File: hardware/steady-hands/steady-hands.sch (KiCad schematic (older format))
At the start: 16 parts, among them J1 SWD, J2 UART, J3 I2C, SW1 SW_Push, SW2 SW_SPDT, U1 STM32F411CEUx

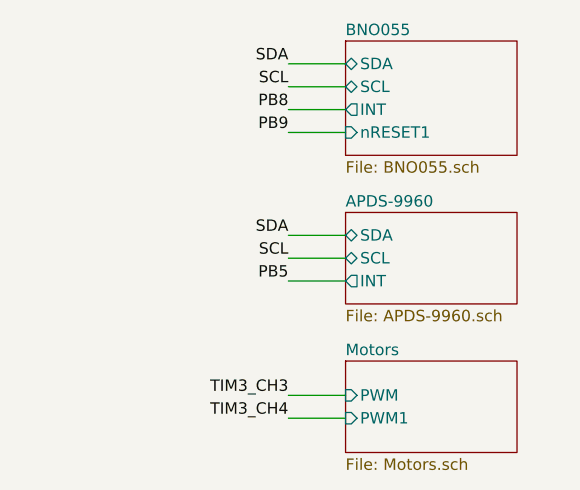
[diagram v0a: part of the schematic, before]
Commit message: Adds footprints
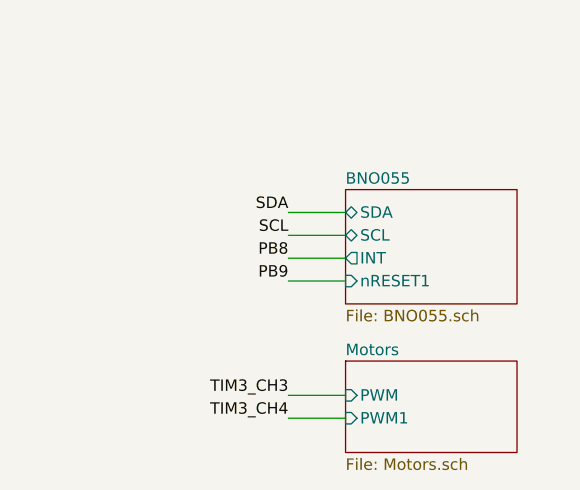
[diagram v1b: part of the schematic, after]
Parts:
- C1, C2, C3, C4, C5, C6, C7, C8, C9: footprint (none) -> Capacitor_SMD:C_0402_1005Metric
- J1: footprint (none) -> Connector_PinHeader_2.54mm:PinHeader_1x04_P2.54mm_Vertical
- J2: footprint (none) -> Connector_PinHeader_2.54mm:PinHeader_1x05_P2.54mm_Vertical
- J3: footprint (none) -> Connector_PinHeader_2.54mm:PinHeader_1x06_P2.54mm_Vertical
- R1: footprint (none) -> Resistor_SMD:R_0402_1005Metric
- SW1: footprint (none) -> Button_Switch_SMD:SW_SPST_B3SL-1002P
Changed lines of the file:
@@
 $Descr A4 11693 8268
 encoding utf-8
-Sheet 1 7
+Sheet 1 6
 Title ""
 Date ""
@@
 TIM3_CH3
 Wire Wire Line
-	9000 1550 8750 1550
-Wire Wire Line
-	9000 1650 8750 1650
-Wire Wire Line
-	9000 1750 8750 1750
-Text Label 8750 1550 2    50   ~ 0
+	9000 2200 8750 2200
+Wire Wire Line
+	9000 2300 8750 2300
+Wire Wire Line
+	9000 2400 8750 2400
+Text Label 8750 2200 2    50   ~ 0
 SDA
-Text Label 8750 1650 2    50   ~ 0
+Text Label 8750 2300 2    50   ~ 0
 SCL
-Text Label 8750 1750 2    50   ~ 0
+Text Label 8750 2400 2    50   ~ 0
 PB8
-$Sheet
-S 9000 2200 750  400
-U 5EF838FE
-F0 "APDS-9960" 50
-F1 "APDS-9960.sch" 50
-F2 "SDA" B L 9000 2300 50
-F3 "SCL" B L 9000 2400 50
-F4 "INT" O L 9000 2500 50
-$EndSheet
-Wire Wire Line
-	9000 2300 8750 2300
-Wire Wire Line
-	9000 2400 8750 2400
-Wire Wire Line
-	9000 2500 8750 2500
-Text Label 8750 2300 2    50   ~ 0
-SDA
-Text Label 8750 2400 2    50   ~ 0
-SCL
-Text Label 8750 2500 2    50   ~ 0
-PB5
 $Comp
 L MCU_ST_STM32F4:STM32F411CEUx U1
@@
 PB4
 Wire Wire Line
-	9000 1850 8750 1850
-Text Label 8750 1850 2    50   ~ 0
+	9000 2500 8750 2500
+Text Label 8750 2500 2    50   ~ 0
 PB9
 Wire Wire Line
@@
 F 0 "C1" H 2015 3746 50  0000 L CNN
 F 1 "0.1u" H 2015 3655 50  0000 L CNN
-F 2 "" H 1938 3550 50  0001 C CNN
+F 2 "Capacitor_SMD:C_0402_1005Metric" H 1938 3550 50  0001 C CNN
 F 3 "~" H 1900 3700 50  0001 C CNN
 	1    1900 3700
@@
 F 0 "SW1" V 1446 3652 50  0000 R CNN
 F 1 "SW_Push" V 1355 3652 50  0000 R CNN
-F 2 "" H 1400 3900 50  0001 C CNN
+F 2 "Button_Switch_SMD:SW_SPST_B3SL-1002P" H 1400 3900 50  0001 C CNN
 F 3 "~" H 1400 3900 50  0001 C CNN
 	1    1400 3700
@@
 F 0 "C3" H 2565 4096 50  0000 L CNN
 F 1 "4.7u" H 2565 4005 50  0000 L CNN
-F 2 "" H 2488 3900 50  0001 C CNN
+F 2 "Capacitor_SMD:C_0402_1005Metric" H 2488 3900 50  0001 C CNN
 F 3 "~" H 2450 4050 50  0001 C CNN
 	1    2450 4050
@@
 F 0 "C2" H 2265 1996 50  0000 L CNN
 F 1 "100n" H 2265 1905 50  0000 L CNN
-F 2 "" H 2188 1800 50  0001 C CNN
+F 2 "Capacitor_SMD:C_0402_1005Metric" H 2188 1800 50  0001 C CNN
 F 3 "~" H 2150 1950 50  0001 C CNN
 	1    2150 1950
@@
 F 0 "C4" H 2715 1996 50  0000 L CNN
 F 1 "100n" H 2715 1905 50  0000 L CNN
-F 2 "" H 2638 1800 50  0001 C CNN
+F 2 "Capacitor_SMD:C_0402_1005Metric" H 2638 1800 50  0001 C CNN
 F 3 "~" H 2600 1950 50  0001 C CNN
 	1    2600 1950
@@
 F 0 "C5" H 3165 1996 50  0000 L CNN
 F 1 "100n" H 3165 1905 50  0000 L CNN
-F 2 "" H 3088 1800 50  0001 C CNN
+F 2 "Capacitor_SMD:C_0402_1005Metric" H 3088 1800 50  0001 C CNN
 F 3 "~" H 3050 1950 50  0001 C CNN
 	1    3050 1950
@@
 F 0 "C6" H 3615 1996 50  0000 L CNN
 F 1 "100n" H 3615 1905 50  0000 L CNN
-F 2 "" H 3538 1800 50  0001 C CNN
+F 2 "Capacitor_SMD:C_0402_1005Metric" H 3538 1800 50  0001 C CNN
 F 3 "~" H 3500 1950 50  0001 C CNN
 	1    3500 1950
@@
 F 0 "C7" H 4065 1996 50  0000 L CNN
 F 1 "4.7u" H 4065 1905 50  0000 L CNN
-F 2 "" H 3988 1800 50  0001 C CNN
+F 2 "Capacitor_SMD:C_0402_1005Metric" H 3988 1800 50  0001 C CNN
 F 3 "~" H 3950 1950 50  0001 C CNN
 	1    3950 1950
@@
 F 0 "C8" H 4715 1996 50  0000 L CNN
 F 1 "100n" H 4715 1905 50  0000 L CNN
-F 2 "" H 4638 1800 50  0001 C CNN
+F 2 "Capacitor_SMD:C_0402_1005Metric" H 4638 1800 50  0001 C CNN
 F 3 "~" H 4600 1950 50  0001 C CNN
 	1    4600 1950
@@
 F 0 "C9" H 5165 1996 50  0000 L CNN
 F 1 "1u" H 5165 1905 50  0000 L CNN
-F 2 "" H 5088 1800 50  0001 C CNN
+F 2 "Capacitor_SMD:C_0402_1005Metric" H 5088 1800 50  0001 C CNN
 F 3 "~" H 5050 1950 50  0001 C CNN
 	1    5050 1950
@@
 F 0 "R1" H 2720 5646 50  0000 L CNN
 F 1 "10k" H 2720 5555 50  0000 L CNN
-F 2 "" V 2580 5600 50  0001 C CNN
+F 2 "Resistor_SMD:R_0402_1005Metric" V 2580 5600 50  0001 C CNN
 F 3 "~" H 2650 5600 50  0001 C CNN
 	1    2650 5600
@@
 F 0 "J1" H 7030 2942 50  0000 L CNN
 F 1 "SWD" H 7030 2851 50  0000 L CNN
-F 2 "" H 6950 2950 50  0001 C CNN
+F 2 "Connector_PinHeader_2.54mm:PinHeader_1x04_P2.54mm_Vertical" H 6950 2950 50  0001 C CNN
 F 3 "~" H 6950 2950 50  0001 C CNN
 	1    6950 2950
@@
 F 0 "J2" H 7030 4092 50  0000 L CNN
 F 1 "UART" H 7030 4001 50  0000 L CNN
-F 2 "" H 6950 4050 50  0001 C CNN
+F 2 "Connector_PinHeader_2.54mm:PinHeader_1x05_P2.54mm_Vertical" H 6950 4050 50  0001 C CNN
 F 3 "~" H 6950 4050 50  0001 C CNN
 	1    6950 4050
@@
 F 0 "J3" H 7030 5092 50  0000 L CNN
 F 1 "I2C" H 7030 5001 50  0000 L CNN
-F 2 "" H 6950 5100 50  0001 C CNN
+F 2 "Connector_PinHeader_2.54mm:PinHeader_1x06_P2.54mm_Vertical" H 6950 5100 50  0001 C CNN
 F 3 "~" H 6950 5100 50  0001 C CNN
 	1    6950 5100
@@
 PB8
 $Sheet
-S 9000 1450 750  500
+S 9000 2100 750  500
 U 5EF43BAC
 F0 "BNO055" 50
 F1 "BNO055.sch" 50
-F2 "SDA" B L 9000 1550 50
-F3 "SCL" B L 9000 1650 50
-F4 "INT" O L 9000 1750 50
-F5 "nRESET1" I L 9000 1850 50
+F2 "SDA" B L 9000 2200 50
+F3 "SCL" B L 9000 2300 50
+F4 "INT" O L 9000 2400 50
+F5 "nRESET1" I L 9000 2500 50
 $EndSheet
 $Sheet

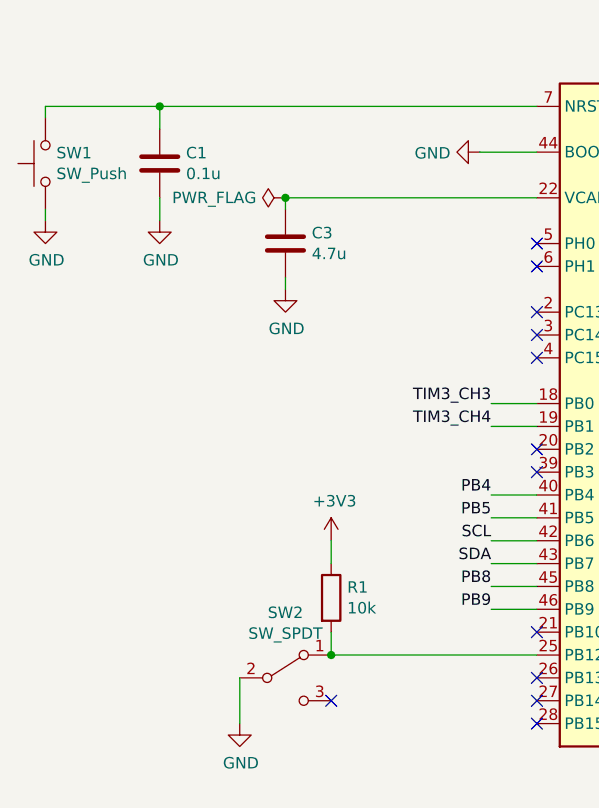
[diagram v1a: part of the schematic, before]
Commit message: Adds all footprints to board
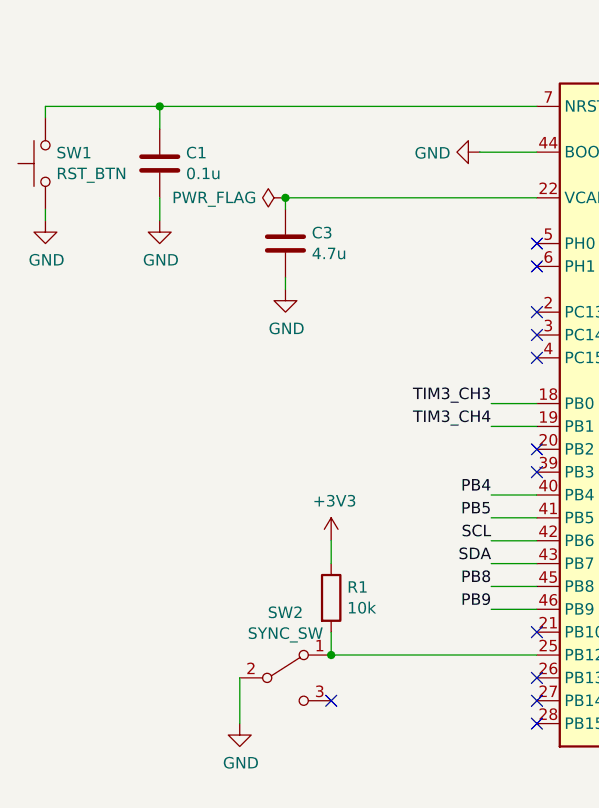
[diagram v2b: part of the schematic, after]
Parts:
- SW1: value SW_Push -> RST_BTN; footprint Button_Switch_SMD:SW_SPST_B3SL-1002P -> Button_Switch_SMD:SW_SPST_B3U-1000P
- SW2: value SW_SPDT -> SYNC_SW; footprint (none) -> Sij_Switches:EG1224
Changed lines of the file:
@@
 P 1400 3700
 F 0 "SW1" V 1446 3652 50  0000 R CNN
-F 1 "SW_Push" V 1355 3652 50  0000 R CNN
-F 2 "Button_Switch_SMD:SW_SPST_B3SL-1002P" H 1400 3900 50  0001 C CNN
+F 1 "RST_BTN" V 1355 3652 50  0000 R CNN
+F 2 "Button_Switch_SMD:SW_SPST_B3U-1000P" H 1400 3900 50  0001 C CNN
 F 3 "~" H 1400 3900 50  0001 C CNN
 	1    1400 3700
@@
 Text Label 5050 5050 0    50   ~ 0
 PA4
-Text Label 5050 4850 0    50   ~ 0
-PA2
 Text Label 5050 5250 0    50   ~ 0
 PA6
@@
 Wire Wire Line
 	4850 4950 5050 4950
-Wire Wire Line
-	4850 4850 5050 4850
 Wire Wire Line
 	3350 4750 3550 4750
@@
 F3 "+1V3" O L 9000 5200 50
 F4 "CE" I L 9000 5800 50
-F5 "1V3_EN" I L 9000 5300 50
-F6 "CHG_EN1" I L 9000 5600 50
-F7 "CHG_EN2" I L 9000 5700 50
-F8 "PGOOD" O L 9000 5500 50
-F9 "CHG" O L 9000 5400 50
+F5 "CHG_EN1" I L 9000 5600 50
+F6 "CHG_EN2" I L 9000 5700 50
+F7 "PGOOD" O L 9000 5500 50
+F8 "CHG" O L 9000 5400 50
+F9 "1V3_EN" I L 9000 5300 50
 $EndSheet
 $Comp
@@
 Text Label 8750 5600 2    50   ~ 0
 PA5
-Text Label 8750 5300 2    50   ~ 0
-PA2
 Text Label 5050 5450 0    50   ~ 0
 PA8
@@
 P 2450 5950
 F 0 "SW2" H 2450 6235 50  0000 C CNN
-F 1 "SW_SPDT" H 2450 6144 50  0000 C CNN
-F 2 "" H 2450 5950 50  0001 C CNN
+F 1 "SYNC_SW" H 2450 6144 50  0000 C CNN
+F 2 "Sij_Switches:EG1224" H 2450 5950 50  0001 C CNN
 F 3 "~" H 2450 5950 50  0001 C CNN
 	1    2450 5950
@@
 Wire Wire Line
 	2650 5850 3550 5850
+Text Label 5050 4850 0    50   ~ 0
+PA2
+Text Label 8750 5300 2    50   ~ 0
+PA2
+Wire Wire Line
+	4850 4850 5050 4850
 $EndSCHEMATC

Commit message: Edits PCB layout
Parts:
- J1: footprint Connector_PinHeader_2.54mm:PinHeader_1x04_P2.54mm_Vertical -> Connector_PinHeader_1.27mm:PinHeader_1x04_P1.27mm_Vertical
- J2: footprint Connector_PinHeader_2.54mm:PinHeader_1x05_P2.54mm_Vertical -> Connector_PinHeader_1.27mm:PinHeader_1x05_P1.27mm_Vertical
- J3: footprint Connector_PinHeader_2.54mm:PinHeader_1x06_P2.54mm_Vertical -> Connector_PinHeader_1.27mm:PinHeader_1x05_P1.27mm_Vertical; symbol Connector_Generic:Conn_01x06 -> Connector_Generic:Conn_01x05
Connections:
- net GND: now also J3.5 (Pin_5); no longer J3.6 (Pin_6)
- net PB5: now also J3.1 (Pin_1); no longer J3.4 (Pin_4)
- net PB8: now also J3.4 (Pin_4); no longer J3.5 (Pin_5)
- net SCL: now also J3.2 (Pin_2); no longer J3.1 (Pin_1)
- net SDA: now also J3.3 (Pin_3); no longer J3.2 (Pin_2)
- net UART1_CTS: now also J2.3 (Pin_3), U1.32 (PA11); no longer J2.4 (Pin_4), U1.33 (PA12)
- net UART1_RTS: now also J2.4 (Pin_4), U1.33 (PA12); no longer J2.3 (Pin_3), U1.32 (PA11)
- net UART1_RX: now also J2.2 (Pin_2), U1.31 (PA10); no longer J2.1 (Pin_1), U1.30 (PA9)
- net UART1_TX: now also J2.1 (Pin_1), U1.30 (PA9); no longer J2.2 (Pin_2), U1.31 (PA10)
- net PA1: now reaches U1.11 (PA1)
- net PA1: now also R1.2, SW2.1 (A)
- net PB4: no longer names the net of U1.40 (PB4)
- net PB4: no longer J3.3 (Pin_3)
- now unconnected: U1.25 (PB12)
- no-connect marks 15 -> 16
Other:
- moved on the sheet: R1, SW2
